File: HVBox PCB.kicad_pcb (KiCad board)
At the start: 2 copper layers, 64 x 59 mm, 18 parts, among them IC1 AS78L05RTR-E1, J1 43650-0516, J2 43650-0216, J3 43650-0416, J4 43650-0516, J7 43650-0216, K1 HVR1B12

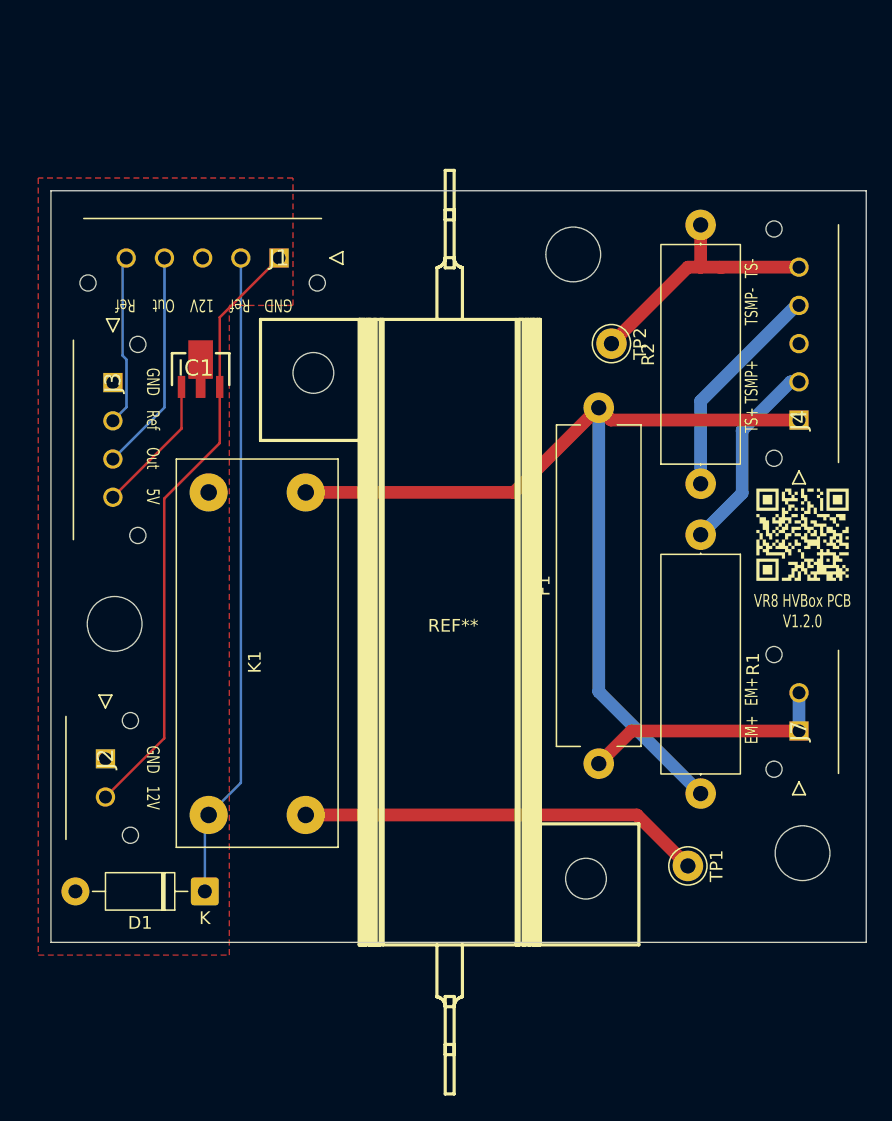
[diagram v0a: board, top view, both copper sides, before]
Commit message: fix: mismatch of schema and pcb
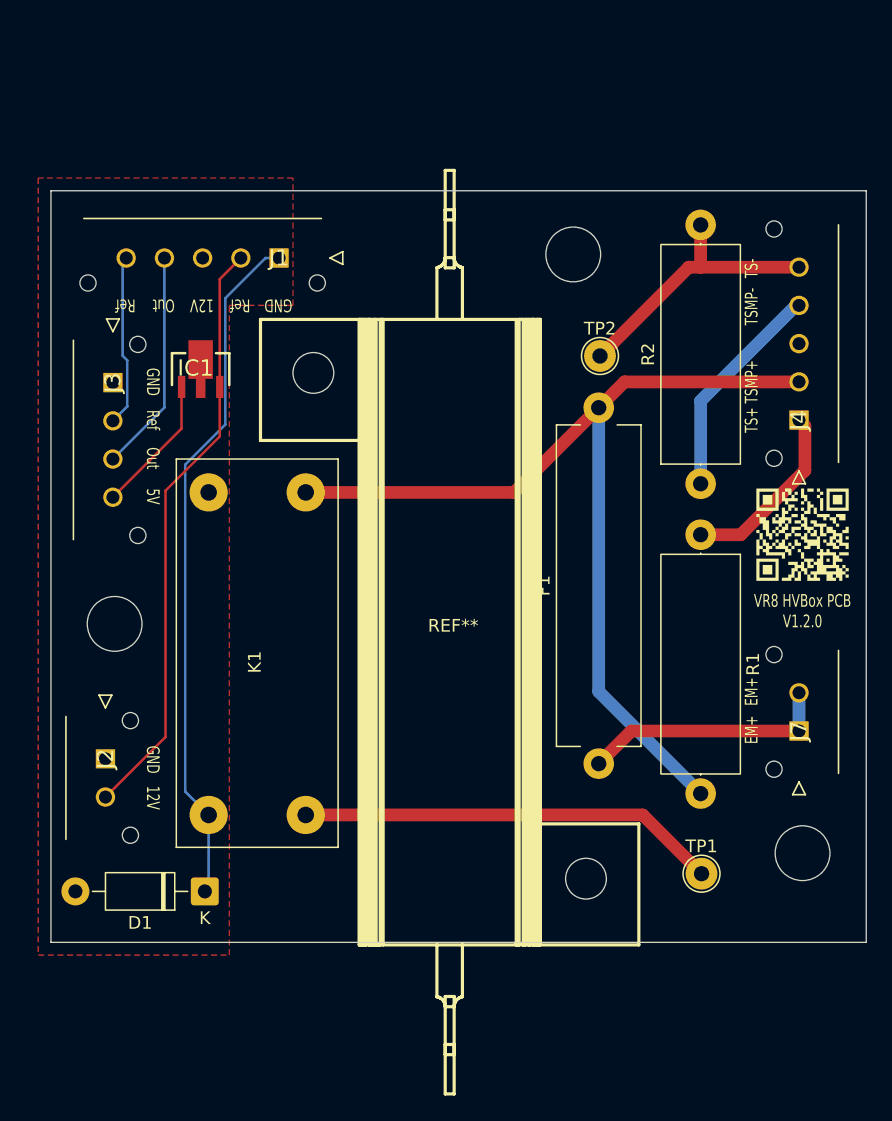
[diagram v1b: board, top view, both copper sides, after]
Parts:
- TP1, TP2: footprint Connector_Pin:Pin_D1.0mm_L10.0mm_LooseFit -> TestPoint:TestPoint_THTPad_D2.5mm_Drill1.2mm
- moved TP2 1.32 mm to (173.1, 93.9), turned to 0 degrees
- moved TP1 1.23 mm to (181.1, 134.5), turned to 0 degrees
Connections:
- J1 pad 1: +12V -> SDC
- J1 pad 2: SDC -> +12V
- J4 pad 1: TS+ -> TSMP(+)
- J4 pad 2: TSMP(+) -> TS+
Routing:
- net SDC: track 50.9 -> 54.3 mm
- net Discharge: track 31.7 -> 33.0 mm
- net TS-: track 20.5 -> 21.8 mm
- net +12V: track 48.0 -> 46.7 mm
- net TSMP(+): track 15.6 -> 14.4 mm

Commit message: better resister position
Move resister from left to right to avoid interference of energy meter.
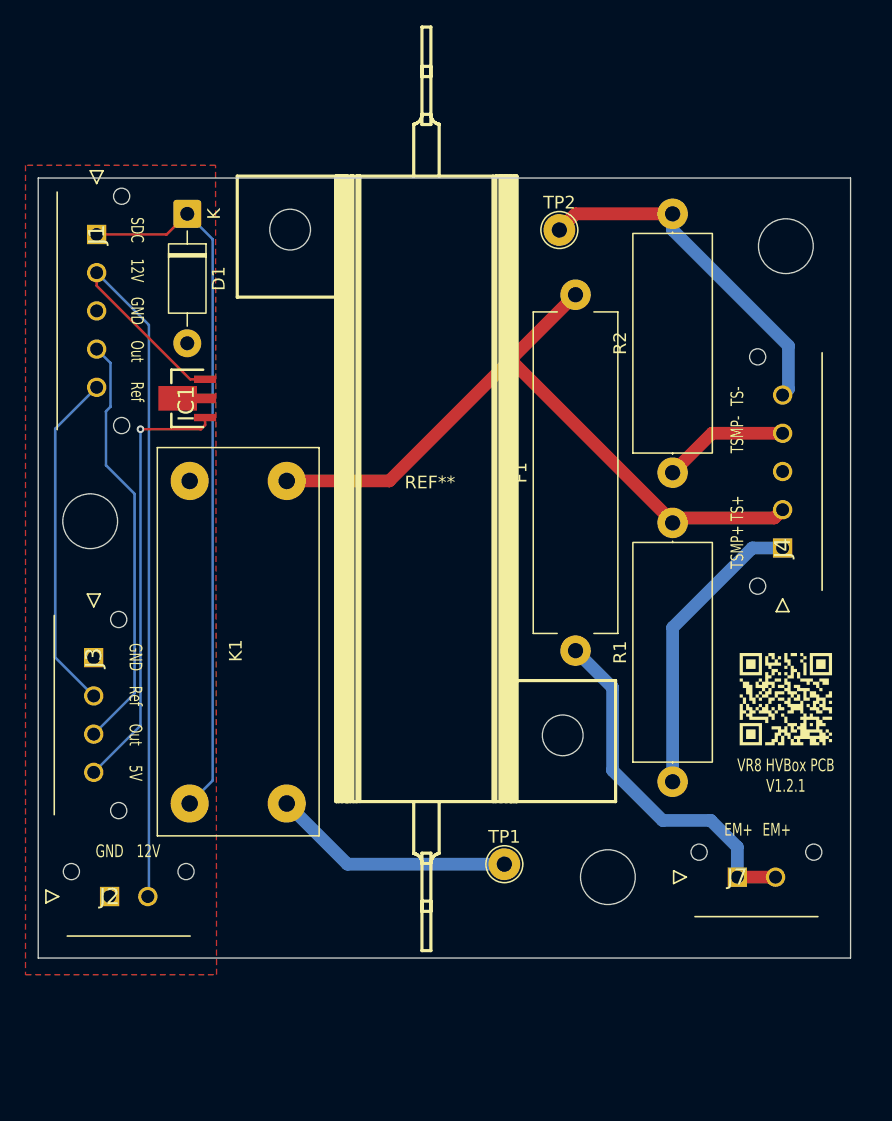
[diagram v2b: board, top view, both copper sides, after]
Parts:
- moved D1 53.2 mm to (140.7, 82.7), turned to -90 degrees
- moved J3 21.6 mm to (133.4, 117.6)
- moved R1 19.5 mm to (178.8, 127.3), turned to 90 degrees
- moved H2 16.7 mm to (187.7, 85.3)
- moved TP1 15.5 mm to (165.6, 133.8)
- moved H3 15.4 mm to (173.7, 134.8)
- moved J1 14.4 mm to (133.6, 84.3), turned to 90 degrees
- moved QR***** 13.0 mm to (187.7, 120.8)
- moved J7 12.5 mm to (183.9, 134.8), turned to 180 degrees
- moved REF** 11.4 mm to (159.8, 104.3)
- moved J2 10.8 mm to (134.6, 136.3), turned to 180 degrees
- moved TP2 10.4 mm to (169.9, 84.0)
- moved J4 10.1 mm to (187.4, 109.0)
- moved F1 9.05 mm to (171.2, 117.0)
- moved H1 8.29 mm to (133.1, 106.9)
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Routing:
- net +5V: track 10.9 -> 34.3 mm, vias 0 -> 1
- net TS+: track 75.9 -> 55.9 mm
- net +12V: track 46.7 -> 63.3 mm
- net Cur_Out: track 17.5 -> 33.1 mm
- net Discharge: track 33.0 -> 19.1 mm
- net Cur_Ref: track 13.5 -> 26.8 mm
- net TSMP(+): track 14.4 -> 23.3 mm
- net Energy Meter(+): track 19.8 -> 28.3 mm
- net TSMP(-): track 17.3 -> 9.92 mm
- net TS-: track 21.8 -> 27.6 mm
- net SDC: track 54.3 -> 55.6 mm
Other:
- board size 64 x 59 mm -> 63.8 x 61.2 mm
- board text added: "GLV"
- board text added: "SDC"
- board text added: "TS"
- board text added: "VR8 HVBox PCB V1.2.1"
- board text removed: "VR8 HVBox PCB V1.2.0"
